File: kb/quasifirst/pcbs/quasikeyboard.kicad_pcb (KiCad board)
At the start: 2 copper layers, 122.5 x 96.3 mm, 24 parts

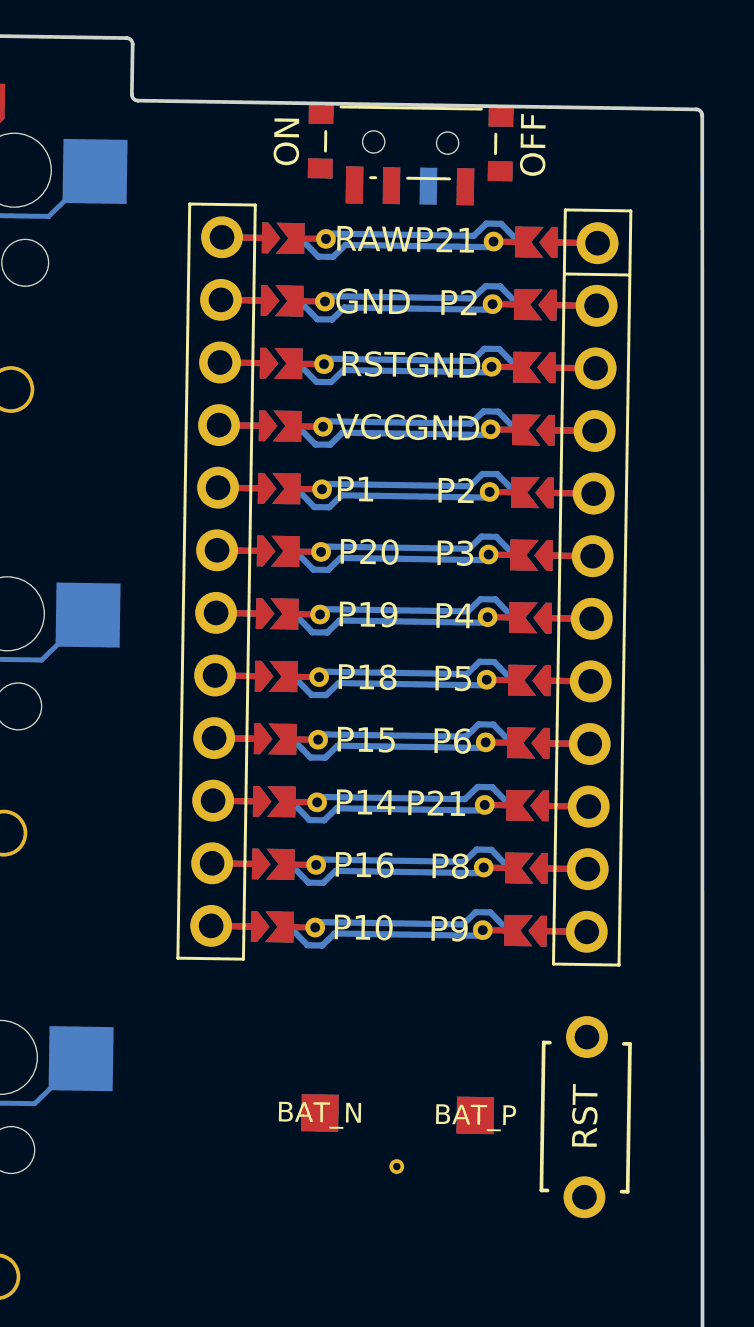
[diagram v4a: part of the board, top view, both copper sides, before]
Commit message: updated the mcu with the extra pins to get thumbs working, worked on the nets and mcu connections
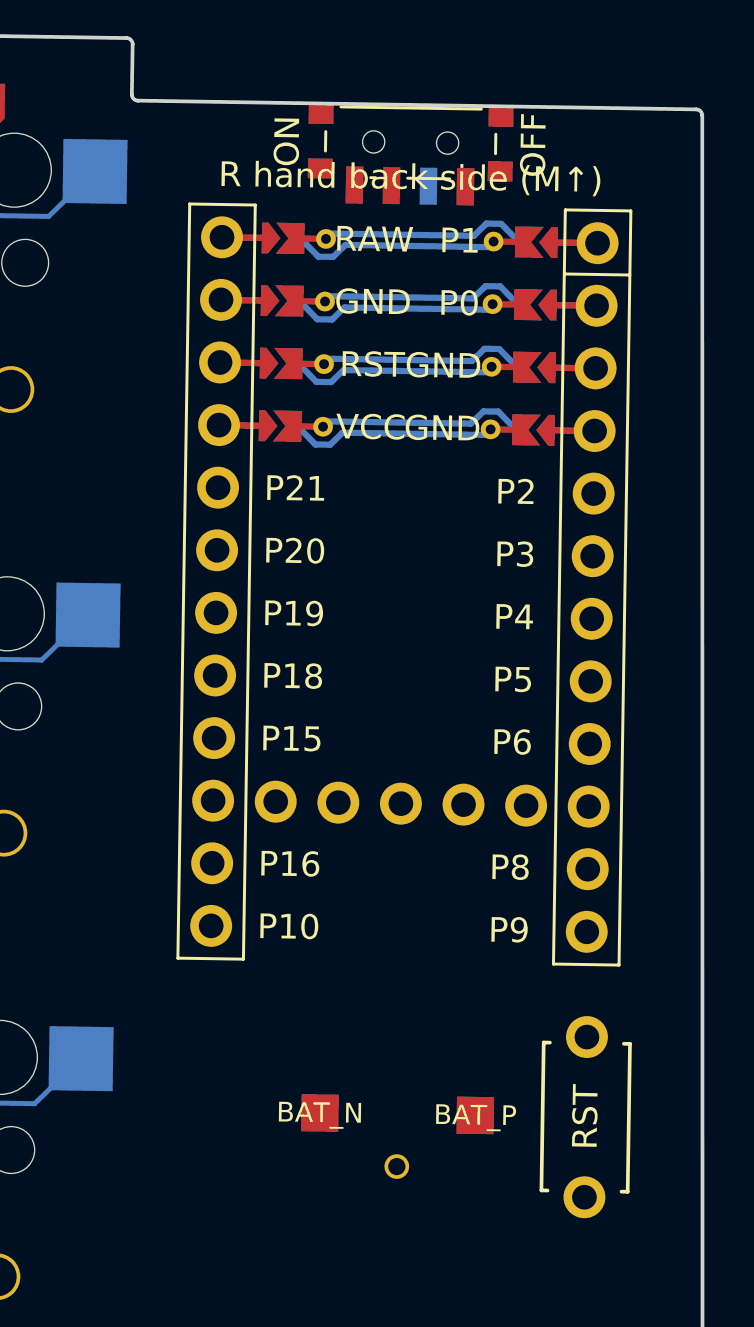
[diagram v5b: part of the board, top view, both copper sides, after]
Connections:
- net MCU1_12 renamed P9
- MCU1 pad 10: MCU1_10 -> matrix_ring_bottom
- MCU1 pad 101: matrix_inner_home -> P1
- MCU1 pad 102: thumb_innit -> P0
- MCU1 pad 11: MCU1_11 -> matrix_pinky_bottom
- MCU1 pad 13: MCU1_13 -> matrix_middle_home
- MCU1 pad 14: MCU1_14 -> matrix_index_home
- MCU1 pad 15: MCU1_15 -> matrix_inner_home
- MCU1 pad 16: MCU1_16 -> matrix_pinky_top
- MCU1 pad 17: MCU1_17 -> matrix_ring_top
- MCU1 pad 18: MCU1_18 -> matrix_middle_top
- MCU1 pad 19: MCU1_19 -> matrix_index_top
- MCU1 pad 20: MCU1_20 -> matrix_inner_top
- MCU1 pad 5: MCU1_5 -> matrix_ring_home
- MCU1 pad 6: MCU1_6 -> matrix_pinky_home
- MCU1 pad 7: MCU1_7 -> matrix_inner_bottom
- MCU1 pad 8: MCU1_8 -> matrix_index_bottom
- MCU1 pad 9: MCU1_9 -> matrix_middle_bottom
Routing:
- net (no net): track 337.7 -> 112.6 mm

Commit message: worked on switches, mcu and little improvements
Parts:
- moved MCU1 0.51 mm to (267.2, 128.2)
- moved PWR1 0.25 mm to (267.5, 111.3)
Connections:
- S1 pad 1: matrix_pinky_bottom -> GND
- S1 pad 2: GND -> matrix_pinky_bottom
- S10 pad 1: matrix_index_bottom -> GND
- S10 pad 2: GND -> matrix_index_bottom
- S11 pad 1: matrix_index_home -> GND
- S11 pad 2: GND -> matrix_index_home
- S12 pad 1: matrix_index_top -> GND
- S12 pad 2: GND -> matrix_index_top
- S13 pad 1: matrix_inner_bottom -> GND
- S13 pad 2: GND -> matrix_inner_bottom
- S14 pad 1: matrix_inner_home -> GND
- S14 pad 2: GND -> matrix_inner_home
- S15 pad 1: matrix_inner_top -> GND
- S15 pad 2: GND -> matrix_inner_top
- S16 pad 1: thumb_innit -> GND
- S16 pad 2: GND -> thumb_innit
- S17 pad 1: thumb_middle -> GND
- S17 pad 2: GND -> thumb_middle
- S18 pad 1: thumb_reachy -> GND
- S18 pad 2: GND -> thumb_reachy
- S2 pad 1: matrix_pinky_home -> GND
- S2 pad 2: GND -> matrix_pinky_home
- S3 pad 1: matrix_pinky_top -> GND
- S3 pad 2: GND -> matrix_pinky_top
- S4 pad 1: matrix_ring_bottom -> GND
- S4 pad 2: GND -> matrix_ring_bottom
- S5 pad 1: matrix_ring_home -> GND
- S5 pad 2: GND -> matrix_ring_home
- S6 pad 1: matrix_ring_top -> GND
- S6 pad 2: GND -> matrix_ring_top
- S7 pad 1: matrix_middle_bottom -> GND
- S7 pad 2: GND -> matrix_middle_bottom
- S8 pad 1: matrix_middle_home -> GND
- S8 pad 2: GND -> matrix_middle_home
- S9 pad 1: matrix_middle_top -> GND
- S9 pad 2: GND -> matrix_middle_top
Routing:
- net GND: track 343.1 -> 120.6 mm
- net matrix_ring_bottom: track 8.27 -> 6.70 mm
- net matrix_ring_top: track 8.27 -> 6.70 mm
- net matrix_ring_home: track 8.27 -> 6.70 mm
- net thumb_reachy: track 8.27 -> 6.70 mm
- net matrix_pinky_home: track 8.27 -> 6.70 mm
- net matrix_pinky_top: track 8.27 -> 6.70 mm
- net matrix_pinky_bottom: track 8.27 -> 6.70 mm
- net thumb_innit: track 8.27 -> 6.70 mm
- net matrix_inner_bottom: track 8.27 -> 6.70 mm
- net matrix_inner_top: track 8.27 -> 6.70 mm
- net matrix_inner_home: track 8.27 -> 6.70 mm
- net thumb_middle: track 8.27 -> 6.70 mm
- net matrix_middle_bottom: track 8.27 -> 6.70 mm
- net matrix_index_bottom: track 8.27 -> 6.70 mm
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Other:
- board text added: "JLCJLCJLCJLCJLC"
